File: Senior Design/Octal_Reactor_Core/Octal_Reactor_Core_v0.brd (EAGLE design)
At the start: 27.9 x 53.2 mm, 61 parts, among them J1 1981584-1, SW1 EG1319, U2 MK20DX256VLH7, U3 MINI54TAN, U5 MCP73831T-2ACI/OT, Y1 32.768kHz (535-9166-2-ND), Y2 16Mhz/8pF, Y3 32.768KHz, Y4 32.768kHz

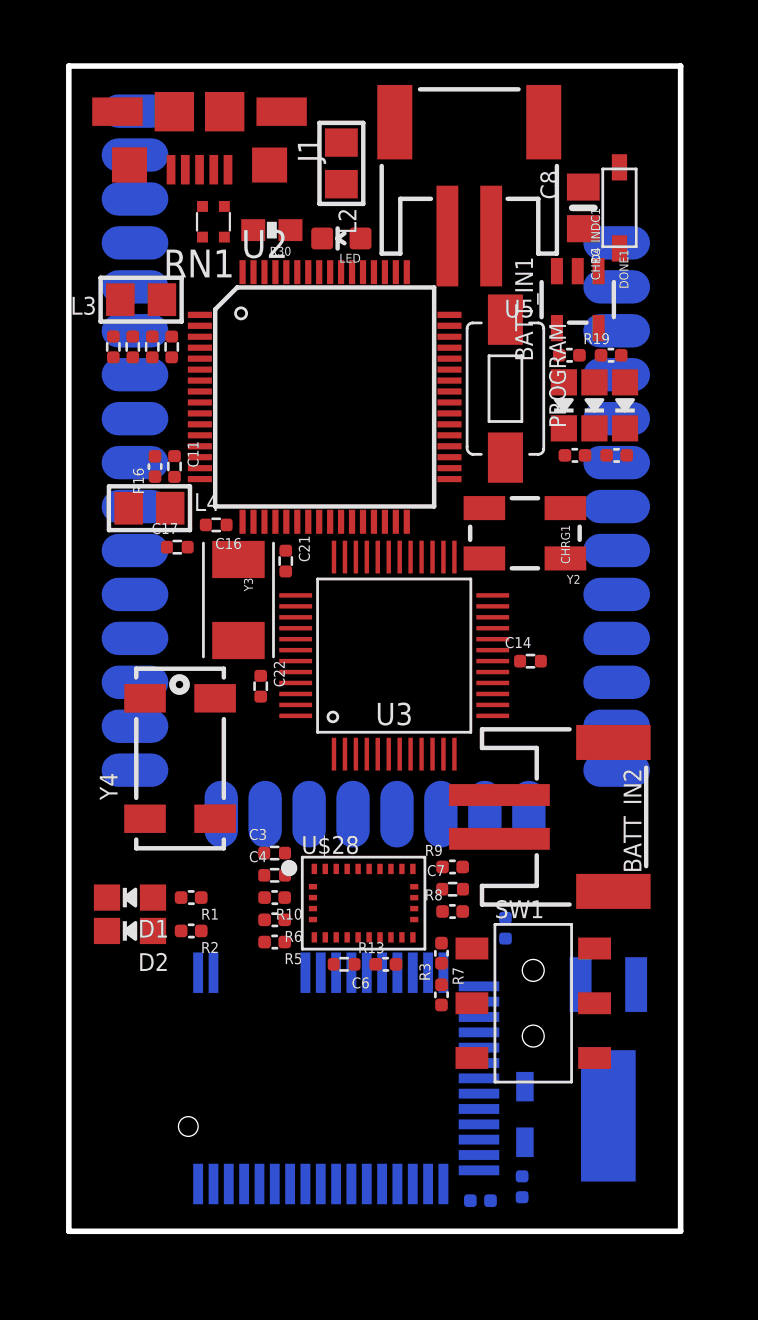
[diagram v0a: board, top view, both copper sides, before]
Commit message: Added Experimental Boards/ Gravity Board/ Home Automation Boards
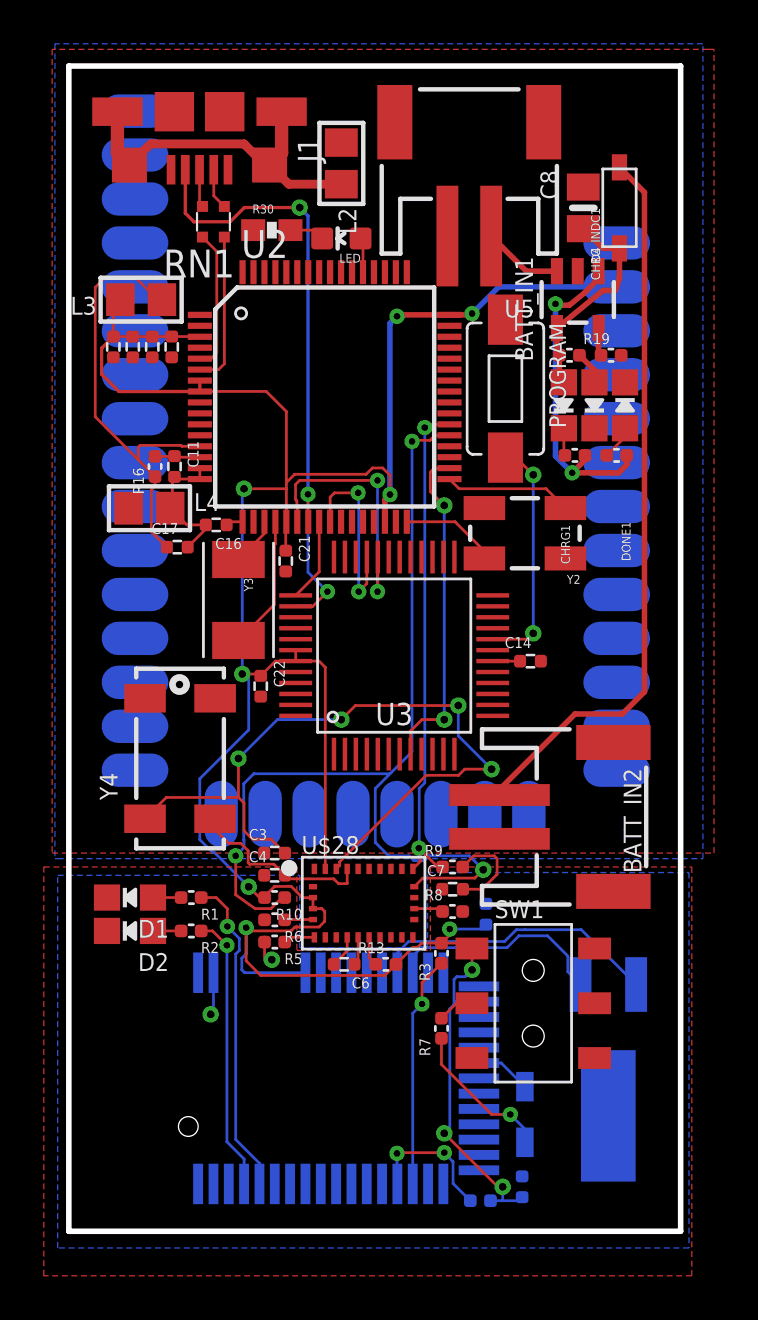
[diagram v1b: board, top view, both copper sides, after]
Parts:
- moved R7 1.52 mm to (17.0, 11.2), turned to 90 degrees
- moved C2 1.09 mm to (19.1, 16.4), turned to 90 degrees
- turned DONE1 to 0 degrees
- turned R30 to 0 degrees
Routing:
- net 3.3V: track 0.00 -> 136.0 mm, vias 0 -> 11
- net SCL: track 0.00 -> 44.7 mm, vias 0 -> 3
- net N$3: track 0.00 -> 34.0 mm, vias 0 -> 4
- net VUSB: track 0.00 -> 33.1 mm
- net ID: track 0.00 -> 28.7 mm, vias 0 -> 3
- net SDA: track 0.00 -> 23.0 mm, vias 0 -> 2
- net VDDA: track 0.00 -> 20.4 mm
- net USB_SHIELD: track 0.00 -> 16.2 mm
- net RESET_B: track 0.00 -> 15.3 mm, vias 0 -> 2
- net N$25: track 0.00 -> 14.9 mm, vias 0 -> 2
- net MODE_LED: track 0.00 -> 14.7 mm, vias 0 -> 1
- net N$1: track 0.00 -> 13.3 mm
- net CONNECTED_LED: track 0.00 -> 12.7 mm, vias 0 -> 1
- net SWD_CLK: track 0.00 -> 12.2 mm, vias 0 -> 2
- net N$19: track 0.00 -> 10.8 mm, vias 0 -> 2
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- added copper zone on layer 1, net GND
- added copper zone on layer 16, net GND
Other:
- board text added: "ALPHA LINE"
- board text added: "MOD #"
- board text added: "OCTAL_CORE v0.1"
